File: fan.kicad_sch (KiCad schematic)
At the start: 36 parts, among them J3 Conn_01x04, J6 Conn_01x04, J7 Conn_01x04, U10 EMC2101, U15 EMC2101, U9 EMC2101

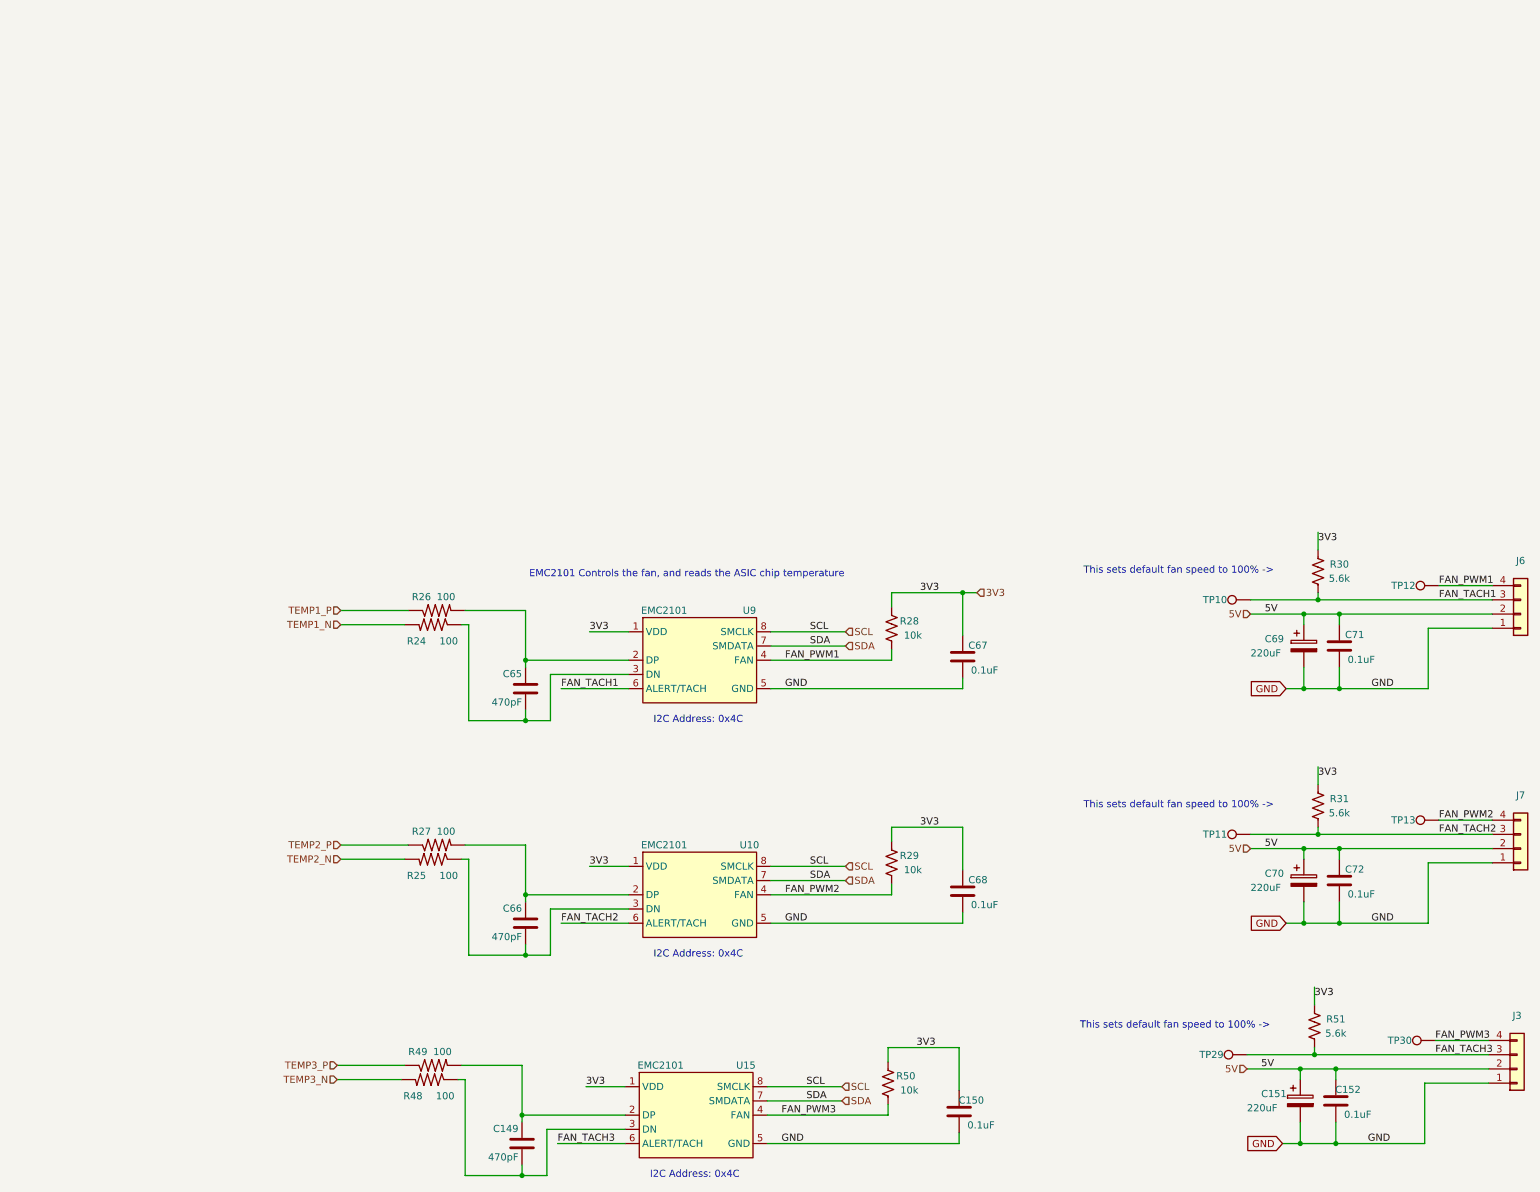
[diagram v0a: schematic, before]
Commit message: update with BM1366
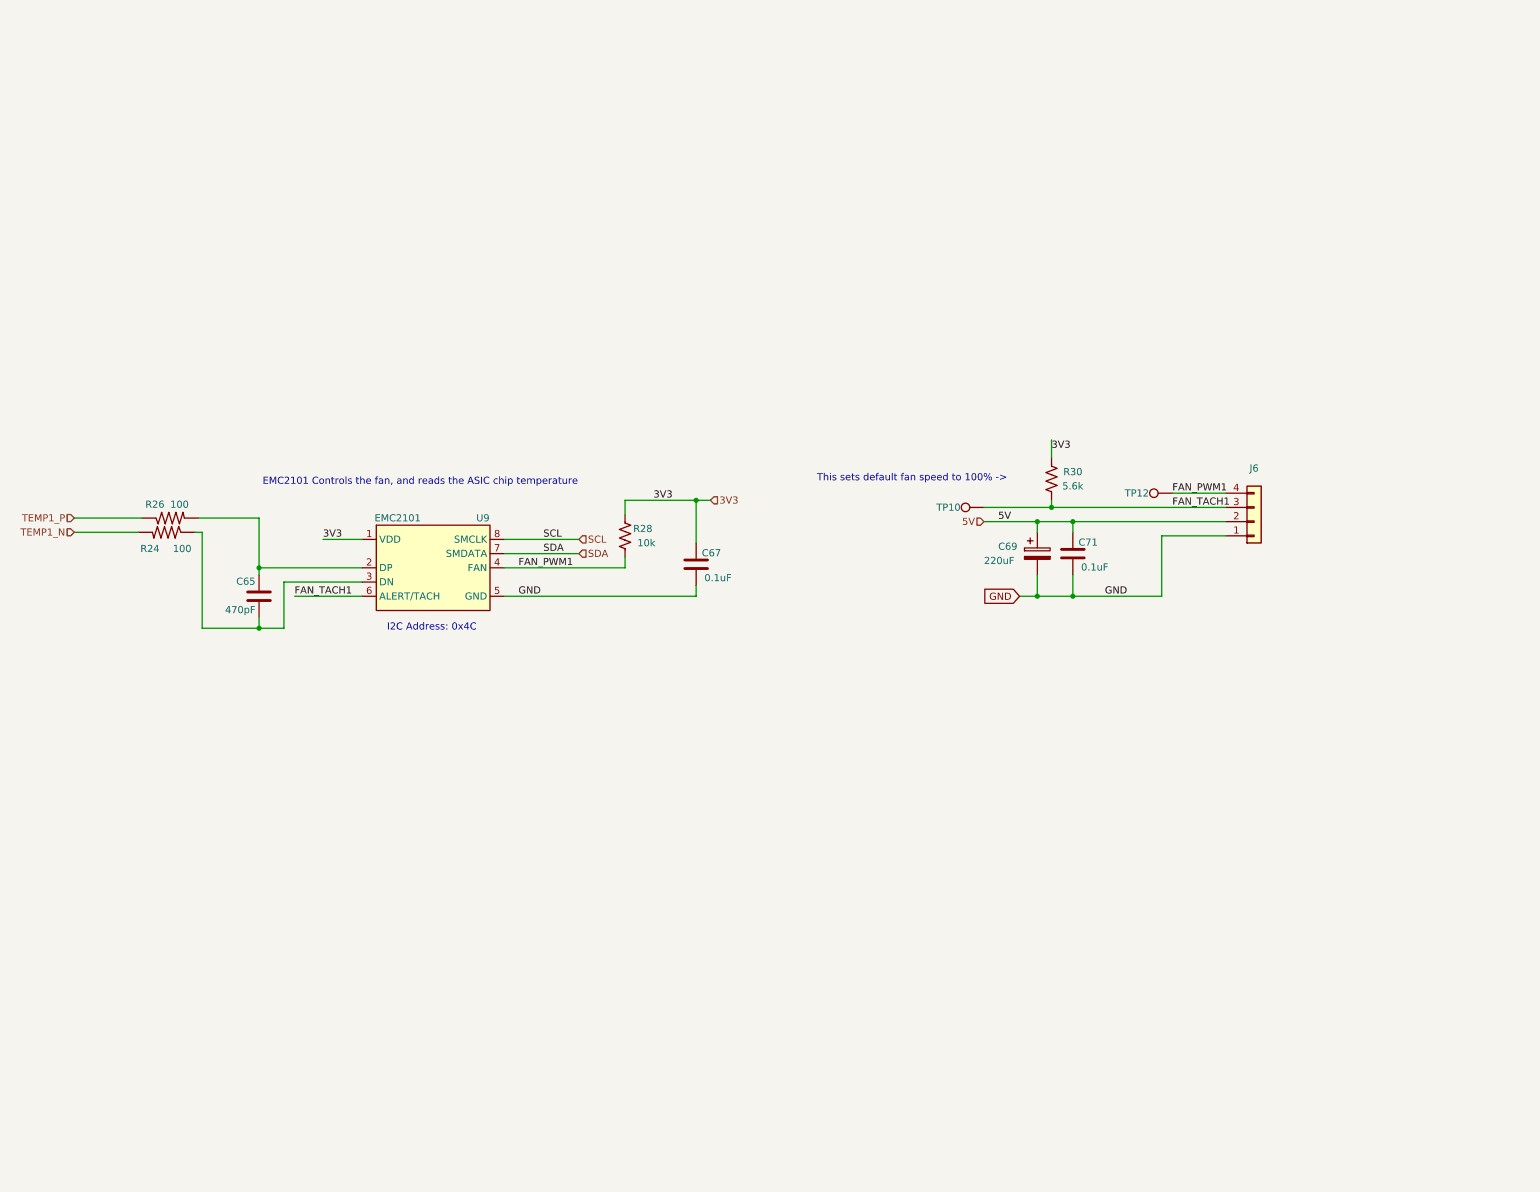
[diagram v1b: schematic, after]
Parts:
- removed C149, C66: 470pF, Capacitor_SMD:C_0402_1005Metric, symbol Device:C
- removed C150, C152, C68, C72: 311-3342-1-ND, Capacitor_SMD:C_0402_1005Metric, symbol Device:C
- removed C151, C70: 220uF, Capacitor_SMD:CP_Elec_6.3x7.7, symbol Device:C_Polarized
- removed J3, J7: Conn_01x04, bitaxe:470531000, symbol Connector_Generic:Conn_01x04
- removed R25, R27, R48, R49: 100, Resistor_SMD:R_0402_1005Metric, symbol DayMiner-eagle-import:RESISTOR0402-RES
- removed R29, R50: 10k, Resistor_SMD:R_0402_1005Metric, symbol Device:R_US
- removed R31, R51: 5.6k, Resistor_SMD:R_0402_1005Metric, symbol Device:R_US
- removed TP11, TP13, TP29, TP30: TestPoint, TestPoint:TestPoint_Pad_D1.5mm, symbol Connector:TestPoint
- removed U10, U15: EMC2101, Package_SO:TSSOP-8_3x3mm_P0.65mm, symbol dayminer:EMC2101
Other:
- moved on the sheet: C65, C67, C69, C71, J6, R24, R26, R28, R30, TP10, TP12, U9

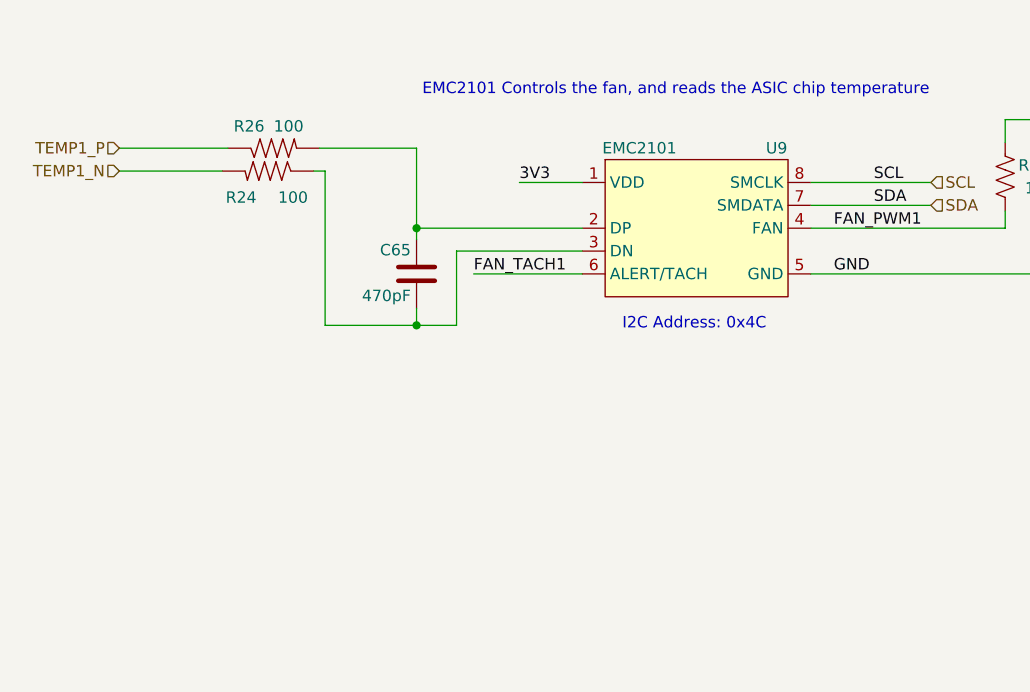
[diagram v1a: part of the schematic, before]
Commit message: cleanup parts and symbol libraries. added TMP1075
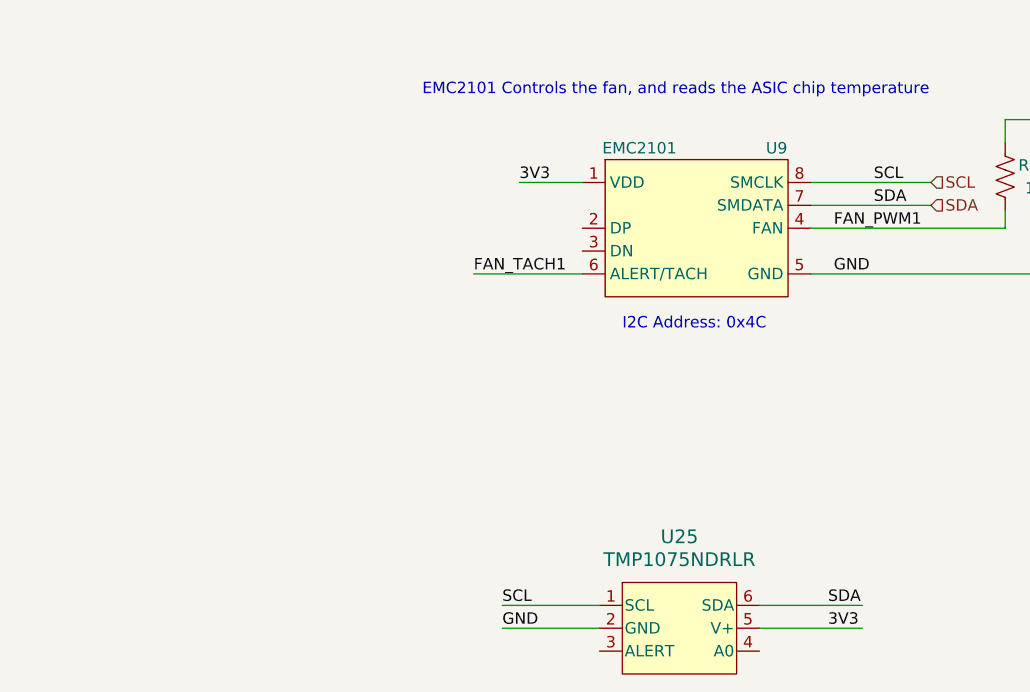
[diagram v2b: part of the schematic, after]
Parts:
- removed C65: 470pF, Capacitor_SMD:C_0402_1005Metric, symbol Device:C
- removed R24, R26: 100, Resistor_SMD:R_0402_1005Metric, symbol DayMiner-eagle-import:RESISTOR0402-RES
- added U25: TMP1075NDRLR, bitaxe:SOT5X3-6_DRL_TEX, symbol bitaxe:TMP1075NDRLR
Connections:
- net 3V3: now also U25.5 (V+)
- net GND: now also U25.2 (GND)
- net SCL: now also U25.1 (SCL)
- net SDA: now also U25.6 (SDA)
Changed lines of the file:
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@@
 (kicad_sch (version 20230121) (generator eeschema)
   (paper "A")
-  (junction (at 66.04 61.595) (diameter 0) (color 0 0 0 0)
-  )
   (junction (at 144.145 49.53) (diameter 0) (color 0 0 0 0)
   )
@@
   (junction (at 205.105 53.34) (diameter 0) (color 0 0 0 0)
   )
-  (junction (at 66.04 72.39) (diameter 0) (color 0 0 0 0)
-  )
   (junction (at 205.105 66.675) (diameter 0) (color 0 0 0 0)
   )
@@
     (stroke (width 0) (type default))
   )
-  (wire (pts (xy 33.02 55.245) (xy 44.45 55.245))
-    (stroke (width 0) (type default))
-  )
-  (wire (pts (xy 55.88 72.39) (xy 66.04 72.39))
-    (stroke (width 0) (type default))
-  )
   (wire (pts (xy 131.445 49.53) (xy 144.145 49.53))
     (stroke (width 0) (type default))
   )
-  (wire (pts (xy 66.04 52.705) (xy 55.245 52.705))
-    (stroke (width 0) (type default))
-  )
   (wire (pts (xy 146.685 49.53) (xy 144.145 49.53))
     (stroke (width 0) (type default))
   )
-  (wire (pts (xy 33.02 52.705) (xy 45.085 52.705))
-    (stroke (width 0) (type default))
-  )
   (wire (pts (xy 72.39 66.675) (xy 84.455 66.675))
     (stroke (width 0) (type default))
@@
     (stroke (width 0) (type default))
   )
-  (wire (pts (xy 84.455 61.595) (xy 66.04 61.595))
-    (stroke (width 0) (type default))
-  )
   (wire (pts (xy 77.47 56.515) (xy 84.455 56.515))
     (stroke (width 0) (type default))
   )
-  (wire (pts (xy 70.485 72.39) (xy 70.485 64.135))
-    (stroke (width 0) (type default))
-  )
   (wire (pts (xy 144.145 64.77) (xy 144.145 66.675))
     (stroke (width 0) (type default))
   )
-  (wire (pts (xy 55.88 55.245) (xy 54.61 55.245))
-    (stroke (width 0) (type default))
-  )
-  (wire (pts (xy 66.04 61.595) (xy 66.04 62.865))
+  (wire (pts (xy 75.565 106.045) (xy 86.36 106.045))
+    (stroke (width 0) (type default))
+  )
+  (wire (pts (xy 104.14 106.045) (xy 115.57 106.045))
     (stroke (width 0) (type default))
   )
@@
     (stroke (width 0) (type default))
   )
-  (wire (pts (xy 66.04 61.595) (xy 66.04 52.705))
-    (stroke (width 0) (type default))
-  )
   (wire (pts (xy 131.445 49.53) (xy 131.445 52.07))
     (stroke (width 0) (type default))
@@
     (stroke (width 0) (type default))
   )
-  (wire (pts (xy 66.04 72.39) (xy 70.485 72.39))
-    (stroke (width 0) (type default))
-  )
   (wire (pts (xy 131.445 61.595) (xy 131.445 59.69))
     (stroke (width 0) (type default))
@@
     (stroke (width 0) (type default))
   )
-  (wire (pts (xy 55.88 55.245) (xy 55.88 72.39))
-    (stroke (width 0) (type default))
-  )
   (wire (pts (xy 229.235 48.26) (xy 238.76 48.26))
     (stroke (width 0) (type default))
@@
     (stroke (width 0) (type default))
   )
+  (wire (pts (xy 104.14 103.505) (xy 115.57 103.505))
+    (stroke (width 0) (type default))
+  )
   (wire (pts (xy 109.855 66.675) (xy 144.145 66.675))
     (stroke (width 0) (type default))
@@
     (stroke (width 0) (type default))
   )
-  (wire (pts (xy 84.455 64.135) (xy 70.485 64.135))
-    (stroke (width 0) (type default))
-  )
   (wire (pts (xy 201.93 66.675) (xy 205.105 66.675))
     (stroke (width 0) (type default))
@@
     (stroke (width 0) (type default))
   )
-  (wire (pts (xy 66.04 70.485) (xy 66.04 72.39))
+  (wire (pts (xy 75.565 103.505) (xy 86.36 103.505))
     (stroke (width 0) (type default))
   )
@@
     (effects (font (size 1.27 1.27)) (justify left bottom))
   )
+  (label "GND" (at 75.565 106.045 0) (fields_autoplaced)
+    (effects (font (size 1.27 1.27)) (justify left bottom))
+  )
   (label "FAN_PWM1" (at 112.395 61.595 0) (fields_autoplaced)
+    (effects (font (size 1.27 1.27)) (justify left bottom))
+  )
+  (label "3V3" (at 111.76 106.045 0) (fields_autoplaced)
+    (effects (font (size 1.27 1.27)) (justify left bottom))
+  )
+  (label "SCL" (at 75.565 103.505 0) (fields_autoplaced)
+    (effects (font (size 1.27 1.27)) (justify left bottom))
+  )
+  (label "SDA" (at 111.76 103.505 0) (fields_autoplaced)
     (effects (font (size 1.27 1.27)) (justify left bottom))
   )
@@
     (effects (font (size 1.27 1.27)) (justify right))
   )
-  (hierarchical_label "TEMP1_P" (shape input) (at 33.02 52.705 180) (fields_autoplaced)
-    (effects (font (size 1.27 1.27)) (justify right))
-  )
   (hierarchical_label "SCL" (shape input) (at 123.19 56.515 0) (fields_autoplaced)
     (effects (font (size 1.27 1.27)) (justify left))
-  )
-  (hierarchical_label "TEMP1_N" (shape input) (at 33.02 55.245 180) (fields_autoplaced)
-    (effects (font (size 1.27 1.27)) (justify right))
   )
   (hierarchical_label "SDA" (shape input) (at 123.19 59.055 0) (fields_autoplaced)
@@
     )
   )
-  (symbol (lib_id "DayMiner-eagle-import:RESISTOR0402-RES") (at 50.165 52.705 0) (mirror x) (unit 1)
-    (in_bom yes) (on_board yes) (dnp no)
-    (property "Reference" "R26" (at 45.72 49.53 0)
-      (effects (font (size 1.27 1.27)) (justify left bottom))
-    )
-    (property "Value" "100" (at 50.165 49.53 0)
-      (effects (font (size 1.27 1.27)) (justify left bottom))
-    )
-    (property "Footprint" "Resistor_SMD:R_0402_1005Metric" (at 50.165 52.705 0)
-      (effects (font (size 1.27 1.27)) hide)
-    )
-    (property "Datasheet" "~" (at 50.165 52.705 0)
-      (effects (font (size 1.27 1.27)) hide)
-    )
-    (property "DK" "RMCF0402FT100RCT-ND" (at 50.165 52.705 0)
-      (effects (font (size 1.778 1.5113)) (justify left bottom) hide)
-    )
-    (property "PARTNO" "RMCF0402FT100R" (at 50.165 52.705 0)
-      (effects (font (size 1.27 1.27)) hide)
-    )
-    (pin "1")
-    (pin "2")
-    (instances
-      (project "bitaxeUltraHex"
-        (path "/e63e39d7-6ac0-4ffd-8aa3-1841a4541b55/8e8832ea-6bf1-49d2-b3a5-32a207f555d2"
-          (reference "R26") (unit 1)
-        )
-      )
-    )
-  )
   (symbol (lib_id "Connector_Generic:Conn_01x04") (at 243.84 53.34 0) (mirror x) (unit 1)
     (in_bom yes) (on_board yes) (dnp no) (fields_autoplaced)
@@
     )
   )
-  (symbol (lib_id "Device:C") (at 66.04 66.675 0) (mirror y) (unit 1)
-    (in_bom yes) (on_board yes) (dnp no)
-    (property "Reference" "C65" (at 65.405 64.77 0)
-      (effects (font (size 1.27 1.27)) (justify left bottom))
-    )
-    (property "Value" "470pF" (at 65.405 69.85 0)
-      (effects (font (size 1.27 1.27)) (justify left bottom))
-    )
-    (property "Footprint" "Capacitor_SMD:C_0402_1005Metric" (at 66.04 66.675 0)
-      (effects (font (size 1.27 1.27)) hide)
-    )
-    (property "Datasheet" "" (at 66.04 66.675 0)
-      (effects (font (size 1.27 1.27)) hide)
-    )
-    (property "DK" "1276-1566-1-ND" (at 66.04 66.675 0)
-      (effects (font (size 1.778 1.5113)) (justify left bottom) hide)
-    )
-    (property "PARTNO" "CL05B471KB5NNNC" (at 66.04 66.675 0)
-      (effects (font (size 1.27 1.27)) hide)
-    )
-    (pin "1")
-    (pin "2")
-    (instances
-      (project "bitaxeUltraHex"
-        (path "/e63e39d7-6ac0-4ffd-8aa3-1841a4541b55/8e8832ea-6bf1-49d2-b3a5-32a207f555d2"
-          (reference "C65") (unit 1)
+  (symbol (lib_id "bitaxe:TMP1075NDRLR") (at 74.93 106.045 0) (unit 1)
+    (in_bom yes) (on_board yes) (dnp no) (fields_autoplaced)
+    (property "Reference" "U25" (at 95.25 95.885 0)
+      (effects (font (size 1.524 1.524)))
+    )
+    (property "Value" "TMP1075NDRLR" (at 95.25 98.425 0)
+      (effects (font (size 1.524 1.524)))
+    )
+    (property "Footprint" "bitaxe:SOT5X3-6_DRL_TEX" (at 101.6 118.745 0)
+      (effects (font (size 1.27 1.27) italic) hide)
+    )
+    (property "Datasheet" "https://www.ti.com/lit/ds/symlink/tmp1075.pdf" (at 99.06 92.075 0)
+      (effects (font (size 1.27 1.27) italic) hide)
+    )
+    (pin "1")
+    (pin "2")
+    (pin "3")
+    (pin "4")
+    (pin "5")
+    (pin "6")
+    (instances
+      (project "bitaxeUltraHex"
+        (path "/e63e39d7-6ac0-4ffd-8aa3-1841a4541b55/8e8832ea-6bf1-49d2-b3a5-32a207f555d2"
+          (reference "U25") (unit 1)
         )
       )
@@
         )
       )
-    )
-  )
-  (symbol (lib_id "DayMiner-eagle-import:RESISTOR0402-RES") (at 49.53 55.245 0) (mirror y) (unit 1)
-    (in_bom yes) (on_board yes) (dnp no)
-    (property "Reference" "R24" (at 48.26 58.925 0)
-      (effects (font (size 1.27 1.27)) (justify left bottom))
-    )
-    (property "Value" "100" (at 53.975 58.925 0)
-      (effects (font (size 1.27 1.27)) (justify left bottom))
-    )
-    (property "Footprint" "Resistor_SMD:R_0402_1005Metric" (at 49.53 55.245 0)
-      (effects (font (size 1.27 1.27)) hide)
-    )
-    (property "Datasheet" "~" (at 49.53 55.245 0)
-      (effects (font (size 1.27 1.27)) hide)
-    )
-    (property "DK" "RMCF0402FT100RCT-ND" (at 49.53 55.245 0)
-      (effects (font (size 1.778 1.5113)) (justify left bottom) hide)
-    )
-    (property "PARTNO" "RMCF0402FT100R" (at 49.53 55.245 0)
-      (effects (font (size 1.27 1.27)) hide)
-    )
-    (pin "1")
-    (pin "2")
-    (instances
-      (project "bitaxeUltraHex"
-        (path "/e63e39d7-6ac0-4ffd-8aa3-1841a4541b55/8e8832ea-6bf1-49d2-b3a5-32a207f555d2"
-          (reference "R24") (unit 1)
-        )
-      )
